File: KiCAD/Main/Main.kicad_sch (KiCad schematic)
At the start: 0 parts

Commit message: Basic PWR systems
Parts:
- added U1: STM32H730VBTx, Package_QFP:LQFP-100_14x14mm_P0.5mm, symbol MCU_ST_STM32H7:STM32H730VBTx
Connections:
- new net: U1.10 (VSS), U1.26 (VSS), U1.49 (VSS), U1.74 (VSS), U1.99 (VSS)
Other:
- added sheet Power & USB & Data (Power_Essentials.kicad_sch)
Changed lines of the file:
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@@
 	(generator_version "9.0")
 	(paper "A4")
-	(sheet_instances
-		(path "/"
-			(page "1")
-		)
-	)
-	(embedded_fonts no)
-)

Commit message: Update power modules
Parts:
- removed U1: STM32H730VBTx, Package_QFP:LQFP-100_14x14mm_P0.5mm, symbol MCU_ST_STM32H7:STM32H730VBTx
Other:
- added sheet Microcontroller (MCU.kicad_sch)
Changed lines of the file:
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@@
 	(generator_version "9.0")
 	(paper "A4")
+	(sheet
+		(at 27.94 30.48)
+		(size 38.1 36.83)
+		(exclude_from_sim no)
+		(in_bom yes)
+		(on_board yes)
+		(dnp no)
+		(fields_autoplaced yes)
+		(stroke
+			(width 0.1524)
+			(type solid)
+		)
+		(fill
+			(color 0 0 0 0.0000)
+		)
+		(property "Sheetname" "Power & USB & Data"
+			(at 27.94 29.7684 0)
+			(effects
+				(font
+					(size 1.27 1.27)
+				)
+				(justify left bottom)
+			)
+		)
+		(property "Sheetfile" "Power_Essentials.kicad_sch"
+			(at 27.94 67.8946 0)
+			(effects
+				(font
+					(size 1.27 1.27)
+				)
+				(justify left top)
+			)
+		)
+		(instances
+			(project "Main"
+				(path "/bbb10697-a5dd-43b8-9c6f-4c5919cf3463"
+					(page "2")
+				)
+			)
+		)
+	)
+	(sheet
+		(at 33.02 97.79)
+		(size 34.29 73.66)
+		(exclude_from_sim no)
+		(in_bom yes)
+		(on_board yes)
+		(dnp no)
+		(fields_autoplaced yes)
+		(stroke
+			(width 0.1524)
+			(type solid)
+		)
+		(fill
+			(color 0 0 0 0.0000)
+		)
+		(property "Sheetname" "Microcontroller"
+			(at 33.02 97.0784 0)
+			(effects
+				(font
+					(size 1.27 1.27)
+				)
+				(justify left bottom)
+			)
+		)
+		(property "Sheetfile" "MCU.kicad_sch"
+			(at 33.02 172.0346 0)
+			(effects
+				(font
+					(size 1.27 1.27)
+				)
+				(justify left top)
+			)
+		)
+		(instances
+			(project "Main"
+				(path "/bbb10697-a5dd-43b8-9c6f-4c5919cf3463"
+					(page "3")
+				)
+			)
+		)
+	)
+	(sheet_instances
+		(path "/"
+			(page "1")
+		)
+	)
+	(embedded_fonts no)
+)

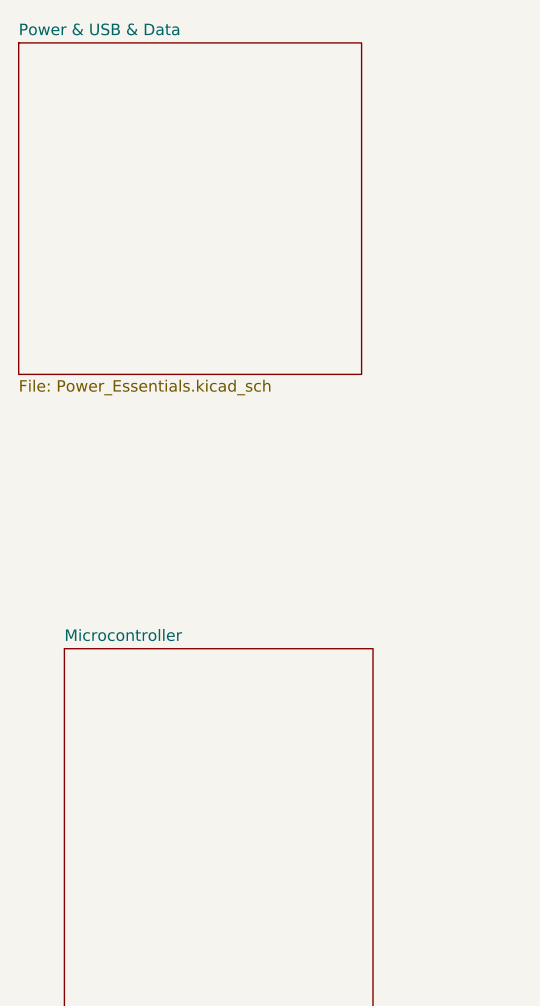
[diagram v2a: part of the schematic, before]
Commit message: Update MCU to display connections
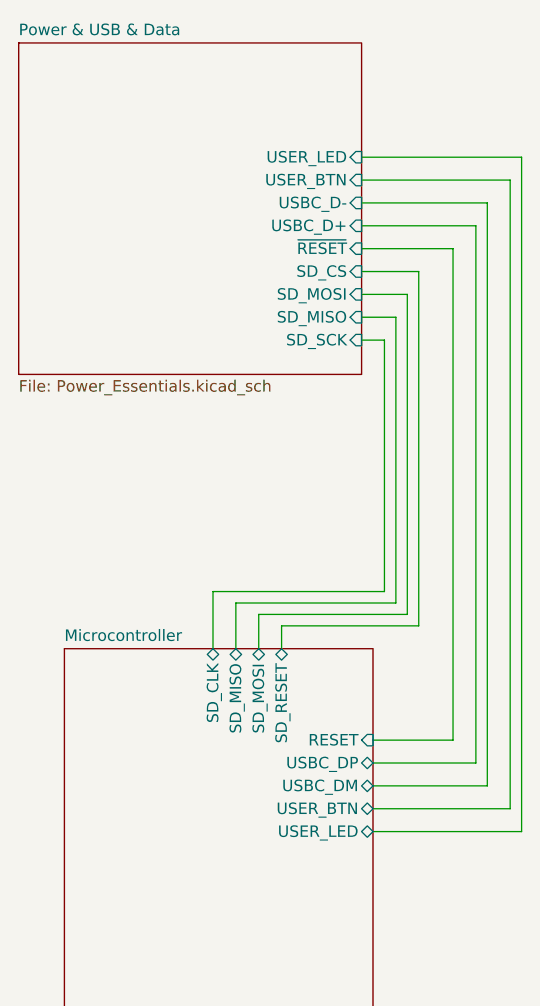
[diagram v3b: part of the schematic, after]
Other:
- sheet Microcontroller ports: added RESET, SD_CLK, SD_MISO, SD_MOSI, SD_RESET, USBC_DM, USBC_DP, USER_BTN, USER_LED; removed none
- sheet Power & USB & Data ports: added SD_CS, SD_MISO, SD_MOSI, SD_SCK, USBC_D+, USBC_D-, USER_BTN, USER_LED, ~{RESET}; removed none

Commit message: Merge GPS to main
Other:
- added sheet GPS (GPS/GPS.kicad_sch)
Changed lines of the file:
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@@
+		)
+	)
+	(sheet
+		(at 95.25 167.64)
+		(size 22.86 24.13)
+		(exclude_from_sim no)
+		(in_bom yes)
+		(on_board yes)
+		(dnp no)
+		(fields_autoplaced yes)
+		(stroke
+			(width 0.1524)
+			(type solid)
+		)
+		(fill
+			(color 0 0 0 0.0000)
+		)
+		(property "Sheetname" "GPS"
+			(at 95.25 166.9284 0)
+			(effects
+				(font
+					(size 1.27 1.27)
+				)
+				(justify left bottom)
+			)
+		)
+		(property "Sheetfile" "GPS/GPS.kicad_sch"
+			(at 95.25 192.3546 0)
+			(effects
+				(font
+					(size 1.27 1.27)
+				)
+				(justify left top)
+			)
+		)
+		(instances
+			(project "Main"
+				(path "/bbb10697-a5dd-43b8-9c6f-4c5919cf3463"
+					(page "4")
+				)
+			)
 		)
 	)

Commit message: Fix labeling issue
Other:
- sheet GPS ports: added GPS_RESET, GPS_UART_RX, GPS_UART_TX; removed none
- sheet Microcontroller ports: added GPS_RESET, GPS_RX, GPS_TX, USER BTN, USER LED; removed USER_BTN, USER_LED
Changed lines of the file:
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@@
+	(wire
+		(pts
+			(xy 66.04 172.72) (xy 95.25 172.72)
+		)
+		(stroke
+			(width 0)
+			(type default)
+		)
+	)
 	(wire
 		(pts
@@
 	(wire
 		(pts
+			(xy 67.31 118.11) (xy 83.82 118.11)
+		)
+		(stroke
+			(width 0)
+			(type default)
+		)
+	)
+	(wire
+		(pts
 			(xy 66.04 55.88) (xy 72.39 55.88)
 		)
@@
 	(wire
 		(pts
+			(xy 63.5 175.26) (xy 63.5 171.45)
+		)
+		(stroke
+			(width 0)
+			(type default)
+		)
+	)
+	(wire
+		(pts
 			(xy 54.61 93.98) (xy 54.61 97.79)
 		)
@@
 	(wire
 		(pts
+			(xy 69.85 170.18) (xy 95.25 170.18)
+		)
+		(stroke
+			(width 0)
+			(type default)
+		)
+	)
+	(wire
+		(pts
 			(xy 76.2 53.34) (xy 76.2 107.95)
 		)
@@
 	(wire
 		(pts
+			(xy 67.31 115.57) (xy 82.55 115.57)
+		)
+		(stroke
+			(width 0)
+			(type default)
+		)
+	)
+	(wire
+		(pts
 			(xy 82.55 115.57) (xy 82.55 45.72)
 		)
@@
 	(wire
 		(pts
+			(xy 67.31 161.29) (xy 69.85 161.29)
+		)
+		(stroke
+			(width 0)
+			(type default)
+		)
+	)
+	(wire
+		(pts
 			(xy 71.12 58.42) (xy 71.12 93.98)
 		)
@@
 	(wire
 		(pts
+			(xy 69.85 161.29) (xy 69.85 170.18)
+		)
+		(stroke
+			(width 0)
+			(type default)
+		)
+	)
+	(wire
+		(pts
 			(xy 66.04 50.8) (xy 78.74 50.8)
 		)
@@
 	(wire
 		(pts
+			(xy 95.25 175.26) (xy 63.5 175.26)
+		)
+		(stroke
+			(width 0)
+			(type default)
+		)
+	)
+	(wire
+		(pts
+			(xy 66.04 171.45) (xy 66.04 172.72)
+		)
+		(stroke
+			(width 0)
+			(type default)
+		)
+	)
+	(wire
+		(pts
 			(xy 80.01 48.26) (xy 80.01 113.03)
 		)
@@
 		(pts
 			(xy 78.74 110.49) (xy 78.74 50.8)
-		)
-		(stroke
-			(width 0)
-			(type default)
-		)
-	)
-	(wire
-		(pts
-			(xy 67.31 118.11) (xy 83.82 118.11)
-		)
-		(stroke
-			(width 0)
-			(type default)
-		)
-	)
-	(wire
-		(pts
-			(xy 67.31 115.57) (xy 82.55 115.57)
 		)
 		(stroke
@@
 			)
 		)
-		(pin "USER_BTN" bidirectional
+		(pin "GPS_RX" bidirectional
+			(at 66.04 171.45 270)
+			(effects
+				(font
+					(size 1.27 1.27)
+				)
+				(justify left)
+			)
+		)
+		(pin "GPS_TX" bidirectional
+			(at 63.5 171.45 270)
+			(effects
+				(font
+					(size 1.27 1.27)
+				)
+				(justify left)
+			)
+		)
+		(pin "GPS_RESET" input
+			(at 67.31 161.29 0)
+			(effects
+				(font
+					(size 1.27 1.27)
+				)
+				(justify right)
+			)
+		)
+		(pin "USER BTN" input
 			(at 67.31 115.57 0)
 			(effects
@@
 			)
 		)
-		(pin "USER_LED" bidirectional
+		(pin "USER LED" input
 			(at 67.31 118.11 0)
 			(effects
@@
 			)
 		)
+		(pin "GPS_RESET" input
+			(at 95.25 170.18 180)
+			(effects
+				(font
+					(size 1.27 1.27)
+				)
+				(justify left)
+			)
+		)
+		(pin "GPS_UART_RX" input
+			(at 95.25 172.72 180)
+			(effects
+				(font
+					(size 1.27 1.27)
+				)
+				(justify left)
+			)
+		)
+		(pin "GPS_UART_TX" input
+			(at 95.25 175.26 180)
+			(effects
+				(font
+					(size 1.27 1.27)
+				)
+				(justify left)
+			)
+		)

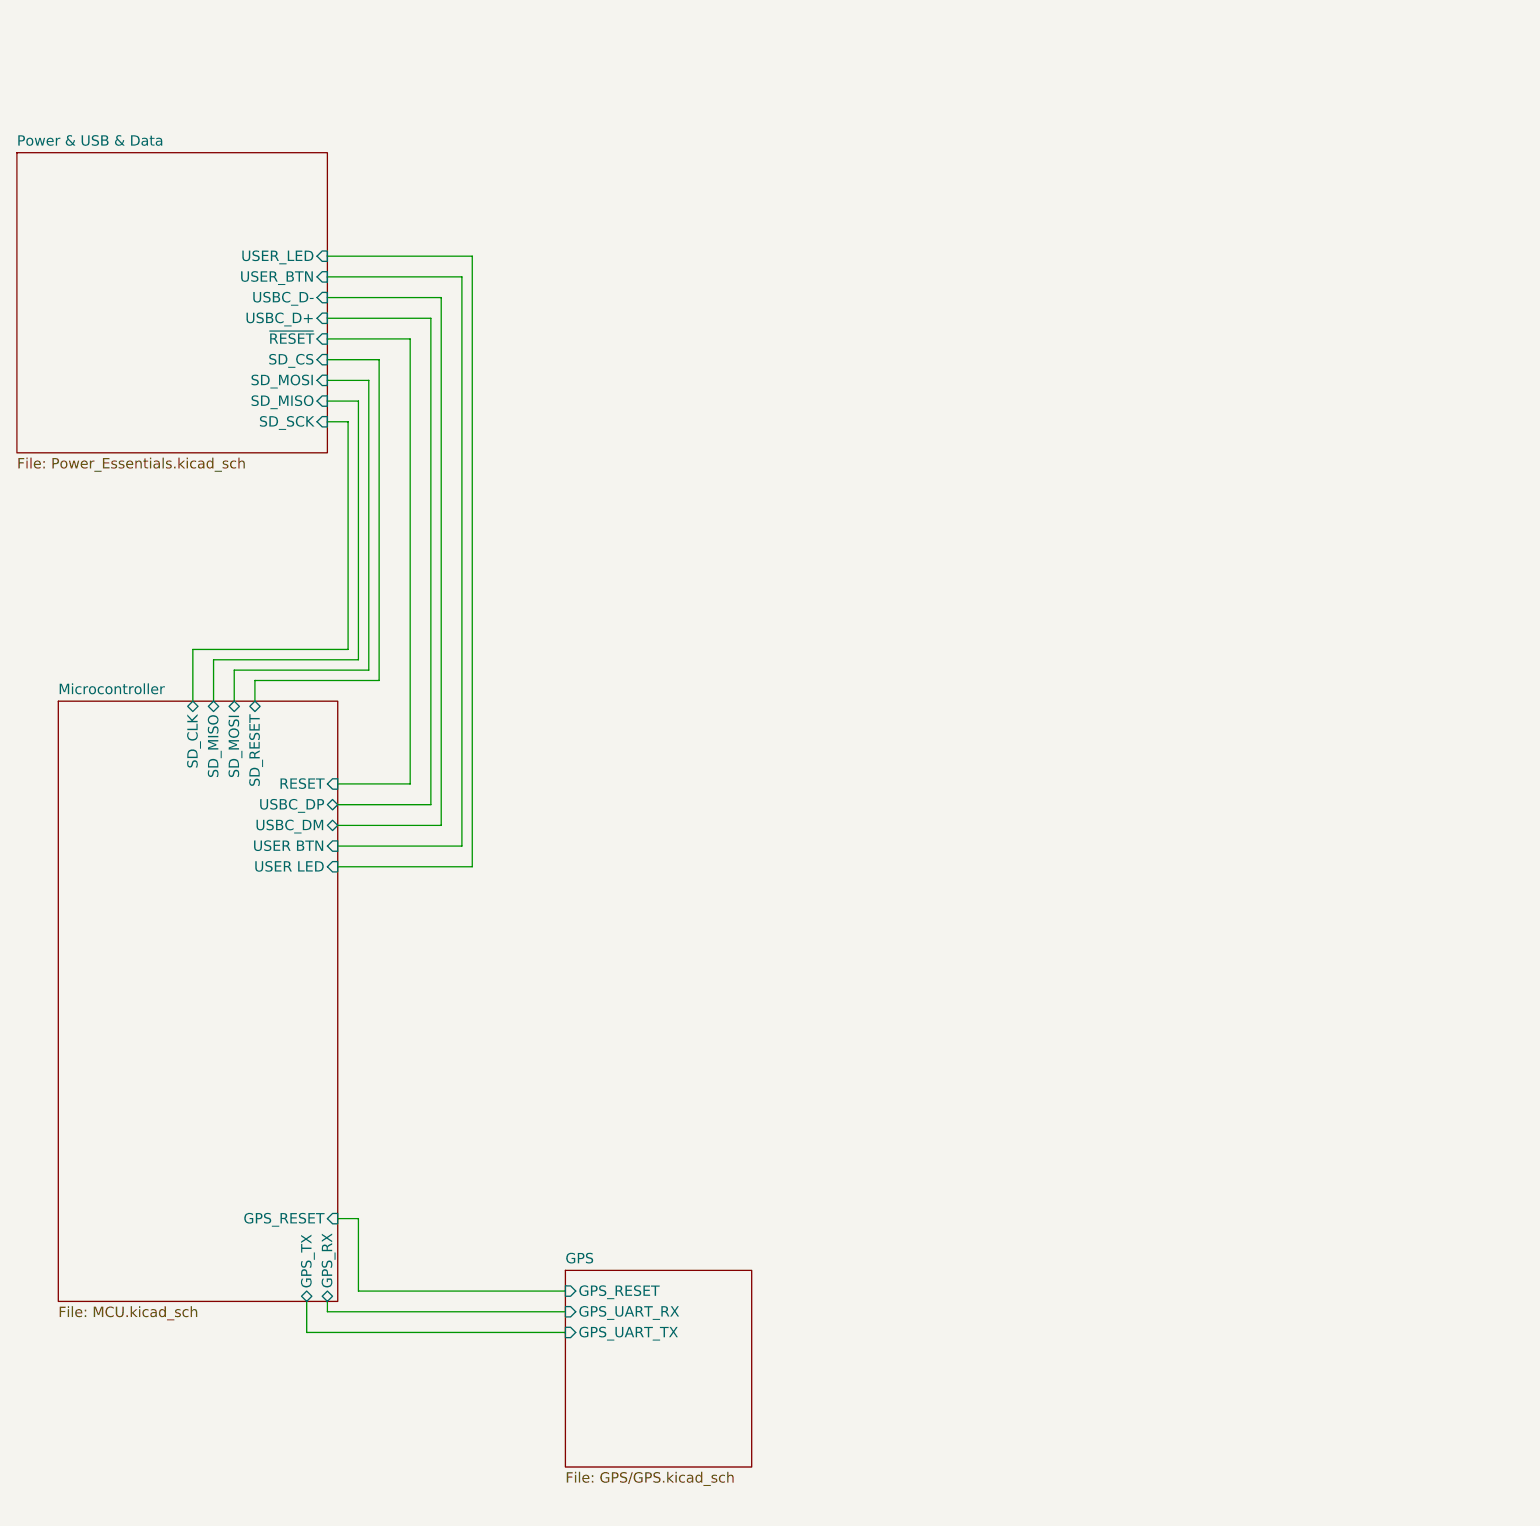
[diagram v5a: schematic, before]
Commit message: Add pin assignments for other sensors
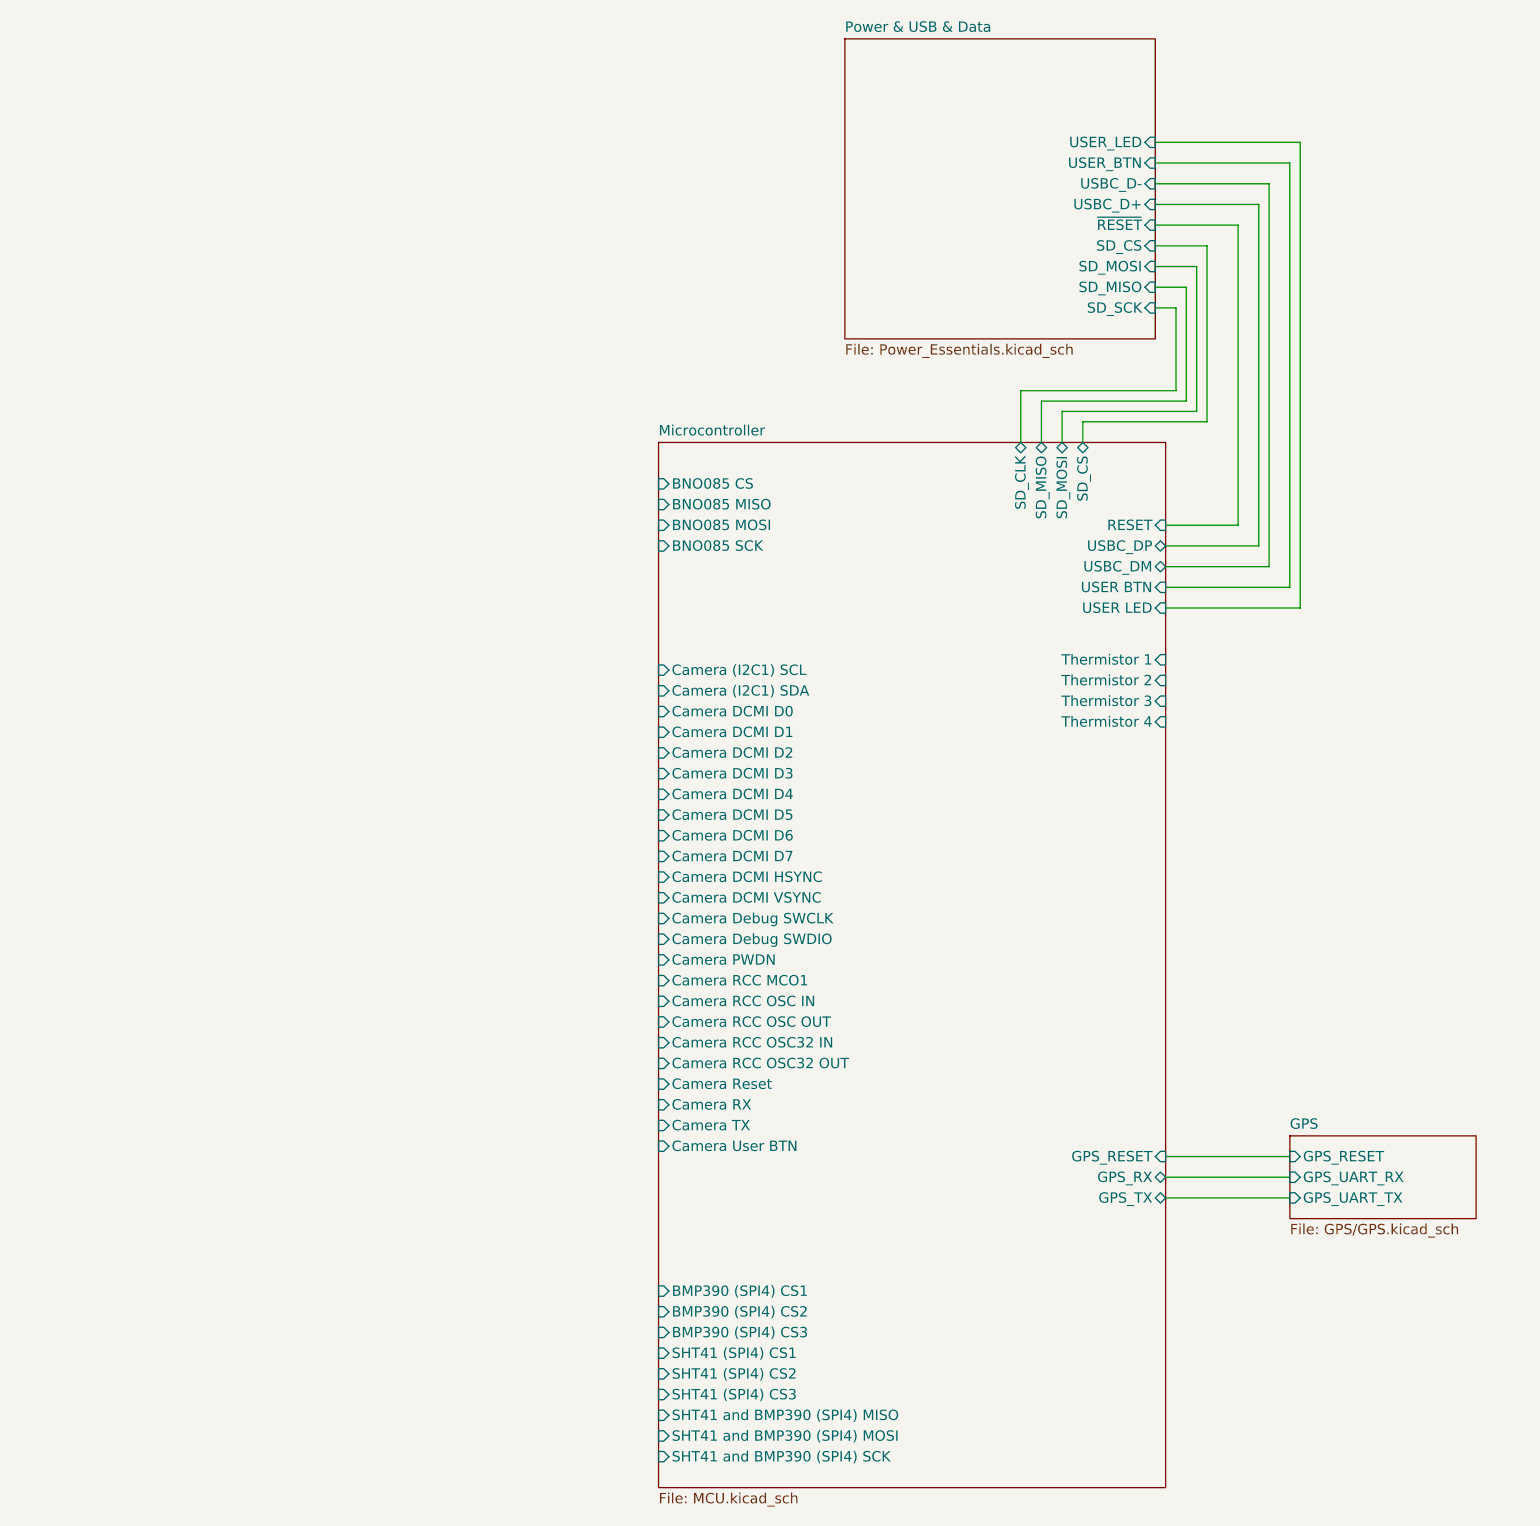
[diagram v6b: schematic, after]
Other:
- sheet Microcontroller ports: added BMP390 (SPI4) CS1, BMP390 (SPI4) CS2, BMP390 (SPI4) CS3, BNO085 CS, BNO085 MISO, BNO085 MOSI, BNO085 SCK, Camera (I2C1) SCL, Camera (I2C1) SDA, Camera DCMI D0, Camera DCMI D1, Camera DCMI D2, Camera DCMI D3, Camera DCMI D4, Camera DCMI D5, Camera DCMI D6, Camera DCMI D7, Camera DCMI HSYNC, Camera DCMI VSYNC, Camera Debug SWCLK, Camera Debug SWDIO, Camera PWDN, Camera RCC MCO1, Camera RCC OSC IN, Camera RCC OSC OUT, Camera RCC OSC32 IN, Camera RCC OSC32 OUT, Camera RX, Camera Reset, Camera TX, Camera User BTN, SD_CS, SHT41 (SPI4) CS1, SHT41 (SPI4) CS2, SHT41 (SPI4) CS3, SHT41 and BMP390 (SPI4) MISO, SHT41 and BMP390 (SPI4) MOSI, SHT41 and BMP390 (SPI4) SCK, Thermistor 1, Thermistor 2, Thermistor 3, Thermistor 4; removed SD_RESET

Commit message: Continue integrating
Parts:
- added J3, J6, J7, J8: Conn_01x02_Socket, symbol Connector:Conn_01x02_Socket
- added U5: LT3092xST, Package_TO_SOT_SMD:SOT-223-3_TabPin2, symbol Reference_Current:LT3092xST
- added U6: ADG5234BRUZ, ADG5234BRUZ:SOP65P640X120-20N, symbol ADG5234BRUZ:ADG5234BRUZ
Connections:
- net Microcontroller/Thermistor 1: now also J3.1 (Pin_1)
- net Microcontroller/Thermistor 2: now also J6.1 (Pin_1)
- net Microcontroller/Thermistor 3: now also J7.1 (Pin_1)
- net Microcontroller/Thermistor 4: now also J8.1 (Pin_1)
- new net GND: U5.1, U6.5 (VSS), U6.6 (GND)
- new net Power & USB & Data/5V_STABILIZED: U5.3, U6.16 (VDD)
- no-connect marks 0 -> 4
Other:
- sheet GPS renamed GPS & Radio
- added sheet Camera (Camera.kicad_sch)
- added sheet IMUs (IMU_CTRLFRK/IMU_CTRLFRK.kicad_sch)
- sheet Power & USB & Data ports: added 3V3_STABILIZED, 5V_STABILIZED; removed none

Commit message: Add files via upload
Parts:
- removed J3, J6, J7, J8: Conn_01x02_Socket, symbol Connector:Conn_01x02_Socket
- removed U5: LT3092xST, Package_TO_SOT_SMD:SOT-223-3_TabPin2, symbol Reference_Current:LT3092xST
- removed U6: ADG5234BRUZ, ADG5234BRUZ:SOP65P640X120-20N, symbol ADG5234BRUZ:ADG5234BRUZ
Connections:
- no-connect marks 4 -> 0
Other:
- removed sheet Camera
- removed sheet GPS & Radio
- removed sheet IMUs
- added sheet RF (RF/RF.kicad_sch)
- sheet Microcontroller ports: added SD_RESET, USER_BTN, USER_LED; removed BMP390 (SPI4) CS1, BMP390 (SPI4) CS2, BMP390 (SPI4) CS3, BNO085 CS, BNO085 MISO, BNO085 MOSI, BNO085 SCK, Camera (I2C1) SCL, Camera (I2C1) SDA, Camera DCMI D0, Camera DCMI D1, Camera DCMI D2, Camera DCMI D3, Camera DCMI D4, Camera DCMI D5, Camera DCMI D6, Camera DCMI D7, Camera DCMI HSYNC, Camera DCMI VSYNC, Camera Debug SWCLK, Camera Debug SWDIO, Camera PWDN, Camera RCC MCO1, Camera RCC OSC IN, Camera RCC OSC OUT, Camera RCC OSC32 IN, Camera RCC OSC32 OUT, Camera RX, Camera Reset, Camera TX, Camera User BTN, GPS_RESET, GPS_RX, GPS_TX, SD_CS, SHT41 (SPI4) CS1, SHT41 (SPI4) CS2, SHT41 (SPI4) CS3, SHT41 and BMP390 (SPI4) MISO, SHT41 and BMP390 (SPI4) MOSI, SHT41 and BMP390 (SPI4) SCK, Thermistor 1, Thermistor 2, Thermistor 3, Thermistor 4, USER BTN, USER LED
- sheet Power & USB & Data ports: added none; removed 3V3_STABILIZED, 5V_STABILIZED
